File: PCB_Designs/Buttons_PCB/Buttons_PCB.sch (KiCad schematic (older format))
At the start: 83 parts, among them P1 CONN_01X05, P2 CONN_01X01, P3 CONN_01X01, P4 CONN_01X01, U1 CHERRY-MX, U10 CHERRY-MX, U11 CHERRY-MX, U12 CHERRY-MX, U13 MCP23017, U14 MCP23017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

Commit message: Main_PCB V1 Complete
Minor changes to everything.
Main_PCB complete with traces and design.
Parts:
- removed P1: CONN_01X05, Socket_Strips:Socket_Strip_Straight_1x05_Pitch2.54mm, symbol CONN_01X05
- added P1: CONN_02X05, Connectors_Multicomp:Multicomp_MC9A22-1034_2x05x2.54mm_Angled, symbol CONN_02X05
- C15: footprint Capacitors_SMD:CP_Elec_4x4.5 -> Capacitors_Tantalum_SMD:CP_Tantalum_Case-A_EIA-3216-18_Reflow
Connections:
- net GND: now also P1.3 (P3), P1.4 (P4)
- net S_CLK_L: now also P1.7 (P7), P1.8 (P8)
- net S_DAT_L: now also P1.5 (P5), P1.6 (P6)
- net VDD: now also P1.1 (P1), P1.2 (P2)
- net intA renamed INT
- net INT: now also P1.10 (P10), P1.9 (P9)
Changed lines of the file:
@@
 	1    0    0    -1
 $EndComp
-Text Label 9000 1600 2    60   ~ 0
+Text Label 8800 1600 2    60   ~ 0
 VDD
-Text Label 9000 1700 2    60   ~ 0
+Text Label 8800 1700 2    60   ~ 0
 GND
-Text Label 9000 1900 2    60   ~ 0
-S_CLK_L
-Text Label 9000 1800 2    60   ~ 0
-S_DAT_L
-Text Label 9000 2100 2    60   ~ 0
-intA
-Text Label 9000 2000 2    60   ~ 0
-intB
 Text Label 6950 1850 0    60   ~ 0
 VDD
@@
 Text Label 6800 6150 0    60   ~ 0
 GND
-Text Label 7300 4850 0    60   ~ 0
-intA
-Text Label 7300 2550 0    60   ~ 0
-intA
-Text Label 7300 2450 0    60   ~ 0
-intB
-Text Label 7300 4750 0    60   ~ 0
-intB
 Text Label 7300 3450 0    60   ~ 0
 GND
@@
 F 0 "C15" H 7200 4100 50  0000 L CNN
 F 1 "4.7u" H 7200 3900 50  0000 L CNN
-F 2 "Capacitors_SMD:CP_Elec_4x4.5" H 7438 3850 50  0001 C CNN
+F 2 "Capacitors_Tantalum_SMD:CP_Tantalum_Case-A_EIA-3216-18_Reflow" H 7438 3850 50  0001 C CNN
 F 3 "" H 7400 4000 50  0000 C CNN
 	1    7400 4000
@@
 	3050 7250 3050 1100
 Wire Notes Line
-	9350 2200 8600 2200
-Wire Notes Line
-	8600 2200 8600 1450
+	9350 2200 8450 2200
+Wire Notes Line
+	8450 2200 8450 1450
 Wire Notes Line
 	8600 1450 9350 1450
@@
 Wire Notes Line
 	10100 2950 10900 2950
-$Comp
-L CONN_01X05 P1
-U 1 1 589F628B
-P 9200 1800
-F 0 "P1" H 9200 2100 50  0000 C CNN
-F 1 "CONN_01X05" V 9300 1800 50  0000 C CNN
-F 2 "Socket_Strips:Socket_Strip_Straight_1x05_Pitch2.54mm" H 9200 1800 50  0001 C CNN
-F 3 "" H 9200 1800 50  0001 C CNN
-	1    9200 1800
-	1    0    0    -1
-$EndComp
-Wire Wire Line
-	9000 2100 9000 2000
 Wire Wire Line
 	4850 4750 4850 3650
@@
 	3300 6750 3400 6750
 Connection ~ 3300 6250
+$Comp
+L CONN_02X05 P1
+U 1 1 58A4C90A
+P 9050 1800
+F 0 "P1" H 9050 2100 50  0000 C CNN
+F 1 "CONN_02X05" H 9050 1500 50  0000 C CNN
+F 2 "Connectors_Multicomp:Multicomp_MC9A22-1034_2x05x2.54mm_Angled" H 9050 600 50  0001 C CNN
+F 3 "" H 9050 600 50  0000 C CNN
+	1    9050 1800
+	1    0    0    -1
+$EndComp
+Wire Wire Line
+	9300 2000 9300 1950
+Wire Wire Line
+	9300 1950 8800 1950
+Wire Wire Line
+	9300 1900 9300 1850
+Wire Wire Line
+	9300 1850 8800 1850
+Wire Wire Line
+	8800 1850 8800 1900
+Wire Wire Line
+	8800 1800 8800 1750
+Wire Wire Line
+	8800 1750 9300 1750
+Wire Wire Line
+	9300 1750 9300 1800
+Wire Wire Line
+	9300 1700 9300 1650
+Wire Wire Line
+	9300 1650 8800 1650
+Wire Wire Line
+	8800 1650 8800 1700
+Wire Wire Line
+	8800 1600 8800 1550
+Wire Wire Line
+	8800 1550 9300 1550
+Wire Wire Line
+	9300 1550 9300 1600
+Text Label 8800 1900 2    60   ~ 0
+S_CLK_L
+Text Label 8800 1800 2    60   ~ 0
+S_DAT_L
+Wire Wire Line
+	7300 2550 7300 2450
+Wire Wire Line
+	7300 4750 7300 4850
+Wire Wire Line
+	8800 1950 8800 2000
+Text Label 8800 2000 2    60   ~ 0
+INT
+Text Label 7300 2550 0    60   ~ 0
+INT
+Text Label 7300 4850 0    60   ~ 0
+INT
 $EndSCHEMATC

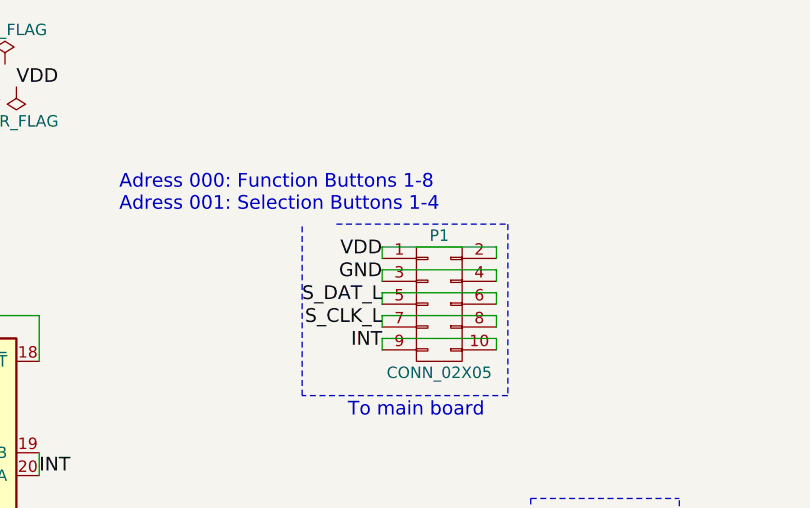
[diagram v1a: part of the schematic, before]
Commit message: Completed all Circuits for evaluation
* All board-to-board connectors now Multicomp 02X05
* Mounting holes for all PCB
* Vias at all groundpins
* Minor other changes
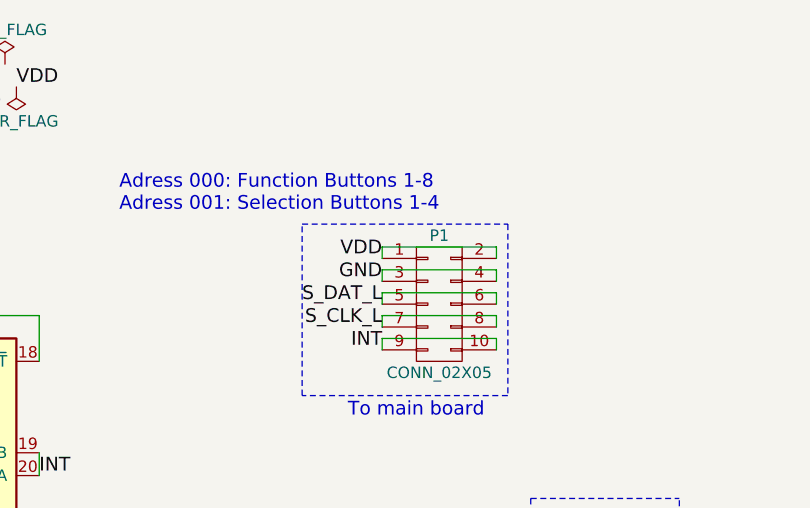
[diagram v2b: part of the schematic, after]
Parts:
- P2, P3, P4: footprint Socket_Strips:Socket_Strip_Straight_1x01_Pitch2.54mm -> Mounting_Holes:MountingHole_2.2mm_M2_DIN965_Pad
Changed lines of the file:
@@
 	8450 2200 8450 1450
 Wire Notes Line
-	8600 1450 9350 1450
+	8450 1450 9350 1450
 Wire Notes Line
 	9350 1450 9350 2200
@@
 F 0 "P2" H 9800 3050 50  0000 C CNN
 F 1 "CONN_01X01" V 9900 2950 50  0000 C CNN
-F 2 "Socket_Strips:Socket_Strip_Straight_1x01_Pitch2.54mm" H 9800 2950 50  0001 C CNN
+F 2 "Mounting_Holes:MountingHole_2.2mm_M2_DIN965_Pad" H 9800 2950 50  0001 C CNN
 F 3 "" H 9800 2950 50  0001 C CNN
 	1    9800 2950
@@
 F 0 "P3" H 9800 3250 50  0000 C CNN
 F 1 "CONN_01X01" V 9900 3150 50  0000 C CNN
-F 2 "Socket_Strips:Socket_Strip_Straight_1x01_Pitch2.54mm" H 9800 3150 50  0001 C CNN
+F 2 "Mounting_Holes:MountingHole_2.2mm_M2_DIN965_Pad" H 9800 3150 50  0001 C CNN
 F 3 "" H 9800 3150 50  0001 C CNN
 	1    9800 3150
@@
 F 0 "P4" H 9800 3450 50  0000 C CNN
 F 1 "CONN_01X01" V 9900 3350 50  0000 C CNN
-F 2 "Socket_Strips:Socket_Strip_Straight_1x01_Pitch2.54mm" H 9800 3350 50  0001 C CNN
+F 2 "Mounting_Holes:MountingHole_2.2mm_M2_DIN965_Pad" H 9800 3350 50  0001 C CNN
 F 3 "" H 9800 3350 50  0001 C CNN
 	1    9800 3350

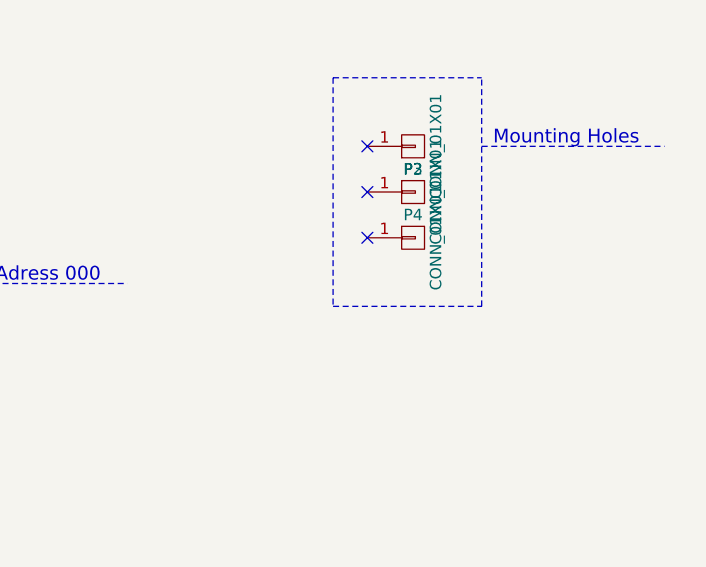
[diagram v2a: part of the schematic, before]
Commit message: Buttons wrong IO expander footprint fixed
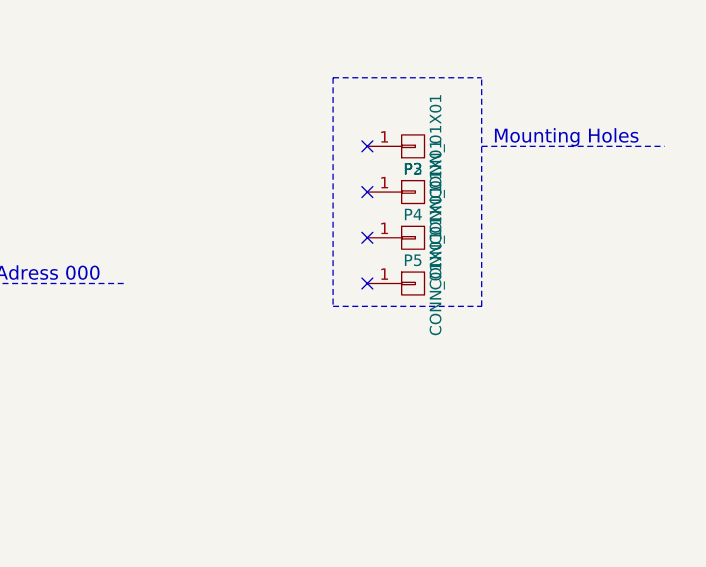
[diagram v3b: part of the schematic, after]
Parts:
- added P5: CONN_01X01, Mounting_Holes:MountingHole_2.2mm_M2_DIN965_Pad, symbol CONN_01X01
- U13, U14: footprint Housings_DIP:DIP-28_W7.62mm_SMDSocket_SmallPads -> Housings_SOIC:SOIC-28W_7.5x17.9mm_Pitch1.27mm
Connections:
- no-connect marks 11 -> 12
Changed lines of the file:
@@
 F 0 "U13" H 6700 3875 50  0000 R CNN
 F 1 "MCP23017" H 6700 3800 50  0000 R CNN
-F 2 "Housings_DIP:DIP-28_W7.62mm_SMDSocket_SmallPads" H 6850 1900 50  0001 L CNN
+F 2 "Housings_SOIC:SOIC-28W_7.5x17.9mm_Pitch1.27mm" H 6850 1900 50  0001 L CNN
 F 3 "" H 7050 3850 50  0001 C CNN
 	1    6800 2850
@@
 F 0 "U14" H 6700 6175 50  0000 R CNN
 F 1 "MCP23017" H 6700 6100 50  0000 R CNN
-F 2 "Housings_DIP:DIP-28_W7.62mm_SMDSocket_SmallPads" H 6850 4200 50  0001 L CNN
+F 2 "Housings_SOIC:SOIC-28W_7.5x17.9mm_Pitch1.27mm" H 6850 4200 50  0001 L CNN
 F 3 "" H 7050 6150 50  0001 C CNN
 	1    6800 5150
@@
 GND
 $Comp
-L PWR_FLAG #FLG01
+L PWR_FLAG #FLG1
 U 1 1 588ED4C3
 P 7150 750
-F 0 "#FLG01" H 7150 825 50  0001 C CNN
+F 0 "#FLG1" H 7150 825 50  0001 C CNN
 F 1 "PWR_FLAG" H 7150 900 50  0000 C CNN
 F 2 "" H 7150 750 50  0001 C CNN
@@
 $EndComp
 $Comp
-L PWR_FLAG #FLG02
+L PWR_FLAG #FLG2
 U 1 1 588ED59B
 P 7200 850
-F 0 "#FLG02" H 7200 925 50  0001 C CNN
+F 0 "#FLG2" H 7200 925 50  0001 C CNN
 F 1 "PWR_FLAG" H 7200 1000 50  0000 C CNN
 F 2 "" H 7200 850 50  0001 C CNN
@@
 Text Label 7300 4850 0    60   ~ 0
 INT
+$Comp
+L CONN_01X01 P5
+U 1 1 58AB2868
+P 9800 3550
+F 0 "P5" H 9800 3650 50  0000 C CNN
+F 1 "CONN_01X01" V 9900 3550 50  0000 C CNN
+F 2 "Mounting_Holes:MountingHole_2.2mm_M2_DIN965_Pad" H 9800 3550 50  0001 C CNN
+F 3 "" H 9800 3550 50  0001 C CNN
+	1    9800 3550
+	1    0    0    -1
+$EndComp
+NoConn ~ 9600 3550
 $EndSCHEMATC

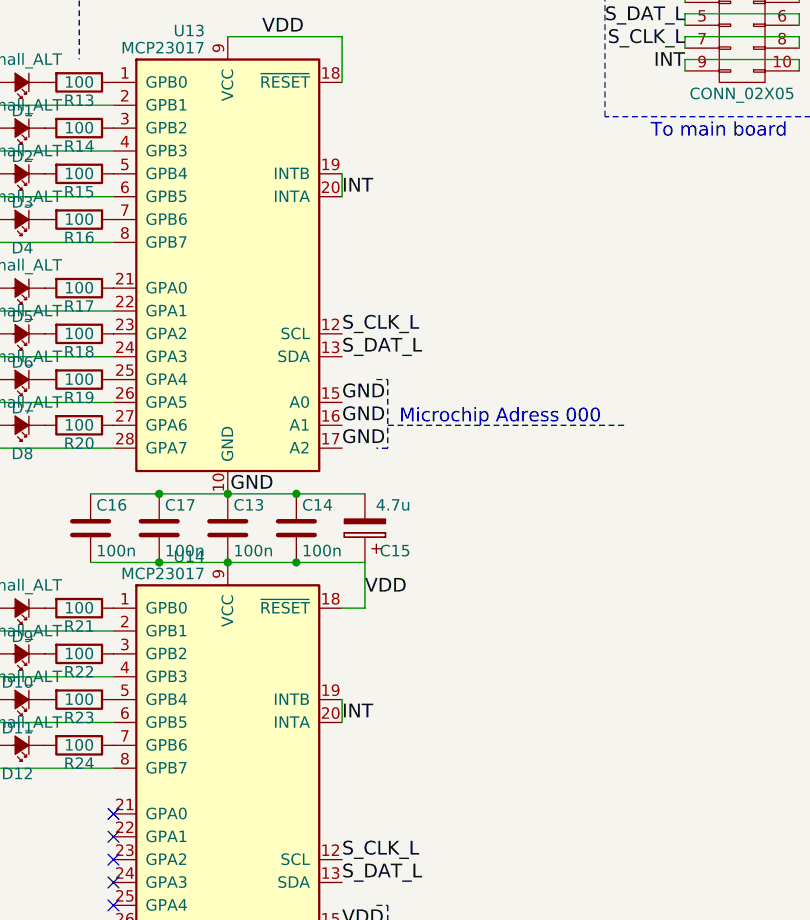
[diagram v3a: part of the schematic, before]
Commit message: Added missing 10k R on OLED board, diodes on Buttons board
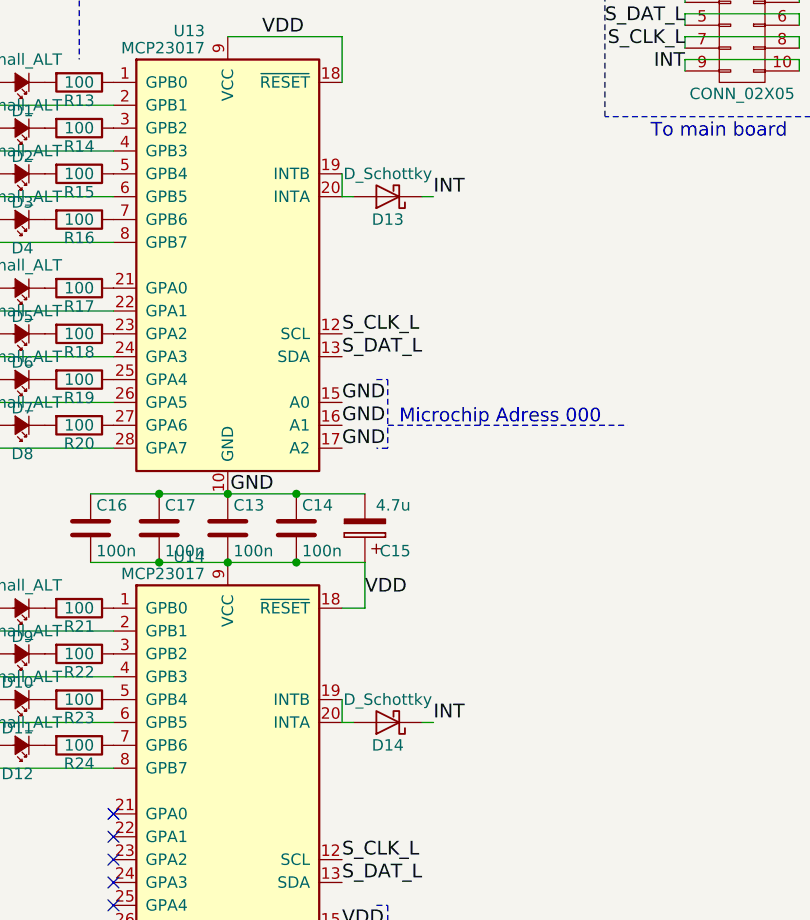
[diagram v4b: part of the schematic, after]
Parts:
- added D13, D14: D_Schottky, Diodes_SMD:D_0603, symbol D_Schottky
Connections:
- net INT: now also D13.1 (K), D14.1 (K); no longer U13.19 (INTB), U13.20 (INTA), U14.19 (INTB), U14.20 (INTA)
- new net: D13.2 (A), U13.19 (INTB), U13.20 (INTA)
- new net: D14.2 (A), U14.19 (INTB), U14.20 (INTA)
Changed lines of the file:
@@
 GND
 $Comp
-L PWR_FLAG #FLG1
+L PWR_FLAG #FLG01
 U 1 1 588ED4C3
 P 7150 750
-F 0 "#FLG1" H 7150 825 50  0001 C CNN
+F 0 "#FLG01" H 7150 825 50  0001 C CNN
 F 1 "PWR_FLAG" H 7150 900 50  0000 C CNN
 F 2 "" H 7150 750 50  0001 C CNN
@@
 $EndComp
 $Comp
-L PWR_FLAG #FLG2
+L PWR_FLAG #FLG02
 U 1 1 588ED59B
 P 7200 850
-F 0 "#FLG2" H 7200 925 50  0001 C CNN
+F 0 "#FLG02" H 7200 925 50  0001 C CNN
 F 1 "PWR_FLAG" H 7200 1000 50  0000 C CNN
 F 2 "" H 7200 850 50  0001 C CNN
@@
 Text Label 8800 2000 2    60   ~ 0
 INT
-Text Label 7300 2550 0    60   ~ 0
+Text Label 7700 2550 0    60   ~ 0
 INT
-Text Label 7300 4850 0    60   ~ 0
+Text Label 7700 4850 0    60   ~ 0
 INT
 $Comp
@@
 $EndComp
 NoConn ~ 9600 3550
+$Comp
+L D_Schottky D14
+U 1 1 58CCF436
+P 7500 4850
+F 0 "D14" H 7500 4950 50  0000 C CNN
+F 1 "D_Schottky" H 7500 4750 50  0000 C CNN
+F 2 "Diodes_SMD:D_0603" H 7500 4850 50  0001 C CNN
+F 3 "" H 7500 4850 50  0001 C CNN
+	1    7500 4850
+	-1   0    0    1
+$EndComp
+Wire Wire Line
+	7300 4850 7350 4850
+Wire Wire Line
+	7650 4850 7700 4850
+$Comp
+L D_Schottky D13
+U 1 1 58CD1AD9
+P 7500 2550
+F 0 "D13" H 7500 2650 50  0000 C CNN
+F 1 "D_Schottky" H 7500 2450 50  0000 C CNN
+F 2 "Diodes_SMD:D_0603" H 7500 2550 50  0001 C CNN
+F 3 "" H 7500 2550 50  0001 C CNN
+	1    7500 2550
+	-1   0    0    1
+$EndComp
+Wire Wire Line
+	7300 2550 7350 2550
+Wire Wire Line
+	7650 2550 7700 2550
 $EndSCHEMATC
